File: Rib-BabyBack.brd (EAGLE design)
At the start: 67.3 x 74.9 mm, 30 parts, among them IC1 REG1117, SW1 DPDT

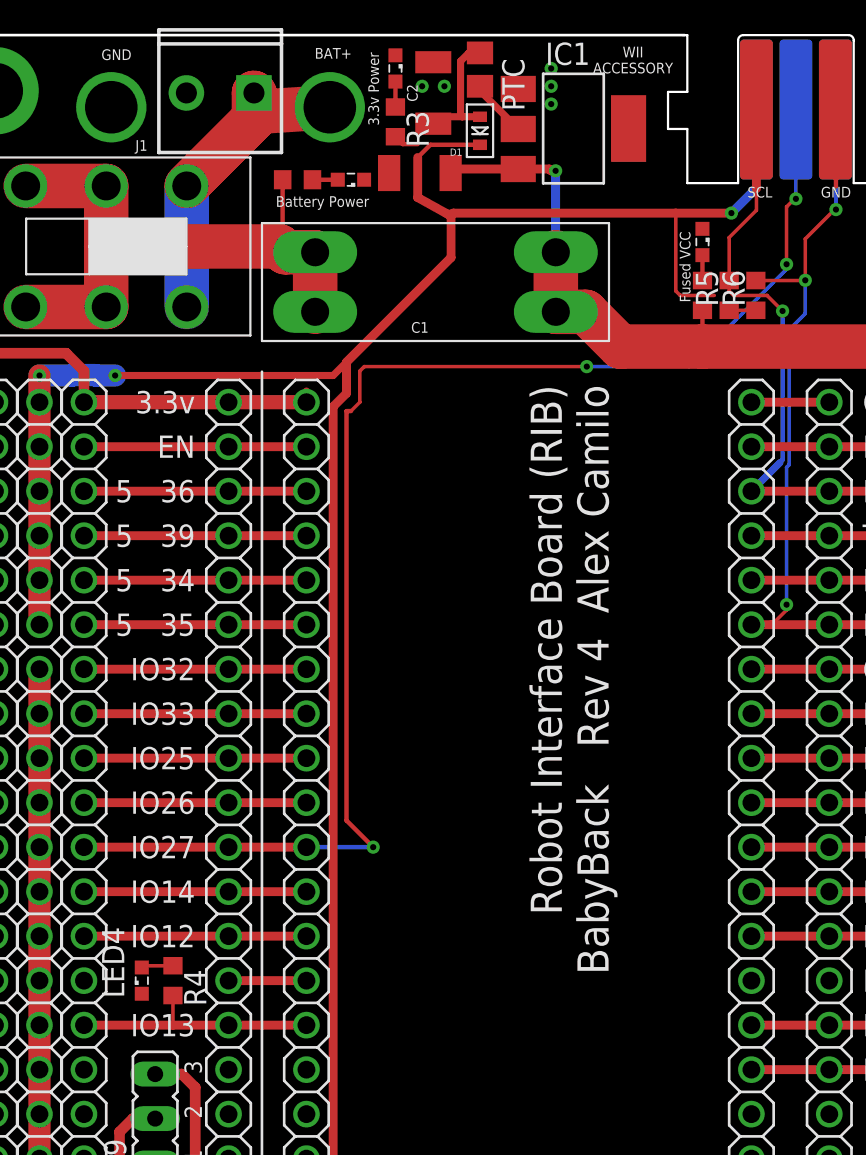
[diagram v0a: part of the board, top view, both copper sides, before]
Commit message: Resolved issue 38
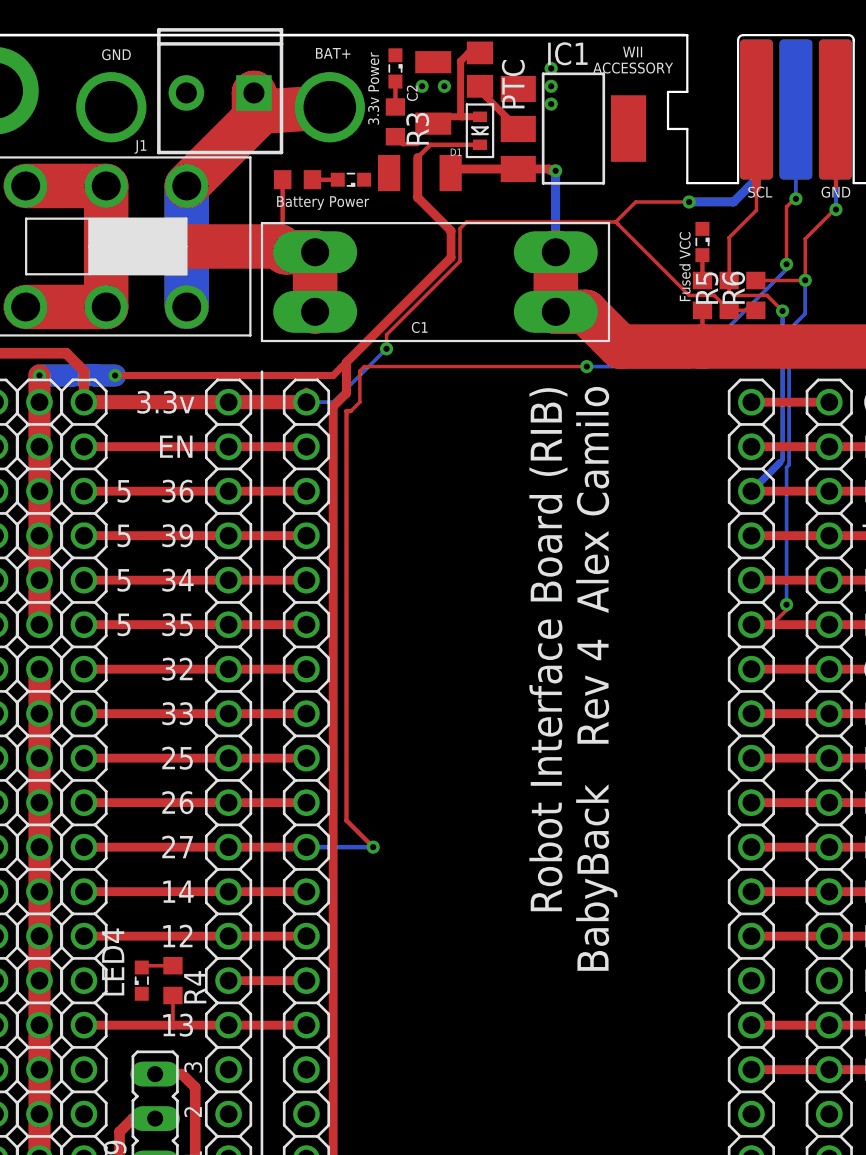
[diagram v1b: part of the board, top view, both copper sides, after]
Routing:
- net 3V3: track 90.1 -> 135.2 mm, vias 0 -> 2
- net 5V: track 141.0 -> 115.8 mm, vias 3 -> 2
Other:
- board text added: "12"
- board text added: "13"
- board text added: "14"
- board text added: "25"
- board text added: "26"
- board text added: "27"
- board text added: "32"
- board text added: "33"
- board text removed: "IO12"
- board text removed: "IO13"
- board text removed: "IO14"
- board text removed: "IO25"
- board text removed: "IO26"
- board text removed: "IO27"
- board text removed: "IO32"
- board text removed: "IO33"
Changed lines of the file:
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@@
 <text x="14.986" y="43.815" size="1.27" layer="21" font="vector" ratio="20" align="bottom-right">34</text>
 <text x="14.986" y="41.275" size="1.27" layer="21" font="vector" ratio="20" align="bottom-right">35</text>
-<text x="14.986" y="38.735" size="1.27" layer="21" font="vector" ratio="20" align="bottom-right">IO32</text>
-<text x="14.986" y="36.195" size="1.27" layer="21" font="vector" ratio="20" align="bottom-right">IO33</text>
-<text x="14.986" y="33.655" size="1.27" layer="21" font="vector" ratio="20" align="bottom-right">IO25</text>
-<text x="14.986" y="31.115" size="1.27" layer="21" font="vector" ratio="20" align="bottom-right">IO26</text>
-<text x="14.986" y="28.575" size="1.27" layer="21" font="vector" ratio="20" align="bottom-right">IO27</text>
-<text x="14.986" y="26.035" size="1.27" layer="21" font="vector" ratio="20" align="bottom-right">IO14</text>
-<text x="14.986" y="23.495" size="1.27" layer="21" font="vector" ratio="20" align="bottom-right">IO12</text>
-<text x="14.986" y="18.415" size="1.27" layer="21" font="vector" ratio="20" align="bottom-right">IO13</text>
+<text x="14.986" y="38.735" size="1.27" layer="21" font="vector" ratio="20" align="bottom-right">32</text>
+<text x="14.986" y="36.195" size="1.27" layer="21" font="vector" ratio="20" align="bottom-right">33</text>
+<text x="14.986" y="33.655" size="1.27" layer="21" font="vector" ratio="20" align="bottom-right">25</text>
+<text x="14.986" y="31.115" size="1.27" layer="21" font="vector" ratio="20" align="bottom-right">26</text>
+<text x="14.986" y="28.575" size="1.27" layer="21" font="vector" ratio="20" align="bottom-right">27</text>
+<text x="14.986" y="26.035" size="1.27" layer="21" font="vector" ratio="20" align="bottom-right">14</text>
+<text x="14.986" y="23.495" size="1.27" layer="21" font="vector" ratio="20" align="bottom-right">12</text>
+<text x="14.986" y="18.415" size="1.27" layer="21" font="vector" ratio="20" align="bottom-right">13</text>
 <text x="14.986" y="8.255" size="1.27" layer="21" font="vector" ratio="20" align="bottom-right">5v</text>
 <text x="53.086" y="53.975" size="1.27" layer="21" font="vector" ratio="20">GND</text>
@@
 <contactref element="JP6" pad="1"/>
 <wire x1="16.891" y1="8.89" x2="21.336" y2="8.89" width="0.508" layer="1"/>
-<wire x1="47.021" y1="66.833" x2="45.593" y2="65.405" width="0.508" layer="16"/>
-<via x="45.593" y="65.405" extent="1-16" drill="0.35"/>
-<wire x1="29.718" y1="65.405" x2="29.6545" y2="65.3415" width="0.508" layer="1"/>
-<wire x1="29.6545" y1="65.3415" x2="29.591" y2="65.278" width="0.508" layer="1"/>
-<wire x1="45.593" y1="65.405" x2="42.418" y2="65.405" width="0.508" layer="1"/>
-<wire x1="42.418" y1="65.405" x2="29.718" y2="65.405" width="0.508" layer="1"/>
-<wire x1="29.6545" y1="65.3415" x2="29.4005" y2="65.3415" width="0.508" layer="1"/>
-<wire x1="29.4005" y1="65.3415" x2="27.686" y2="66.294" width="0.508" layer="1"/>
 <wire x1="27.686" y1="66.294" x2="27.686" y2="68.58" width="0.508" layer="1"/>
 <contactref element="R3" pad="2"/>
@@
 <wire x1="23.622" y1="55.118" x2="23.622" y2="56.896" width="0.508" layer="1"/>
 <wire x1="23.622" y1="56.896" x2="29.591" y2="62.865" width="0.508" layer="1"/>
-<wire x1="29.591" y1="62.865" x2="29.591" y2="65.278" width="0.508" layer="1"/>
-<wire x1="44.616" y1="60.706" x2="42.672" y2="60.706" width="0.2032" layer="1"/>
-<wire x1="42.672" y1="60.706" x2="42.418" y2="60.96" width="0.2032" layer="1"/>
-<wire x1="42.418" y1="60.96" x2="42.418" y2="65.405" width="0.2032" layer="1"/>
 <wire x1="16.891" y1="8.89" x2="14.986" y2="10.795" width="0.6096" layer="1"/>
 <wire x1="14.986" y1="15.494" x2="14.986" y2="10.795" width="0.6096" layer="1"/>
@@
 <wire x1="10.414" y1="56.134" x2="22.86" y2="56.134" width="0.4064" layer="1"/>
 <wire x1="22.86" y1="56.134" x2="23.622" y2="56.896" width="0.4064" layer="1"/>
+<wire x1="29.591" y1="62.865" x2="29.591" y2="64.389" width="0.508" layer="1"/>
+<wire x1="29.591" y1="64.389" x2="27.686" y2="66.294" width="0.508" layer="1"/>
 <wire x1="28.41" y1="69.304" x2="27.686" y2="69.342" width="0" layer="19" extent="1-1"/>
 <wire x1="8.636" y1="8.89" x2="14.986" y2="10.795" width="0" layer="19" extent="1-1"/>
@@
 <wire x1="11.176" y1="5.334" x2="12.7" y2="6.858" width="0.6096" layer="1"/>
 <wire x1="12.7" y1="6.858" x2="12.7" y2="11.176" width="0.6096" layer="1"/>
-<wire x1="46.99" y1="59.856" x2="47.021" y2="71.315" width="0" layer="19" extent="1-16"/>
-<wire x1="21.336" y1="55.245" x2="45.466" y2="59.856" width="0" layer="19" extent="1-1"/>
+<wire x1="45.466" y1="59.856" x2="44.616" y2="60.706" width="0.2032" layer="1"/>
+<wire x1="44.616" y1="60.706" x2="43.18" y2="60.706" width="0.2032" layer="1"/>
+<wire x1="43.18" y1="60.706" x2="39.116" y2="64.77" width="0.2032" layer="1"/>
+<wire x1="39.116" y1="64.77" x2="38.989" y2="64.897" width="0.2032" layer="1"/>
+<wire x1="38.989" y1="64.897" x2="30.48" y2="64.897" width="0.2032" layer="1"/>
+<wire x1="30.48" y1="64.897" x2="30.099" y2="64.516" width="0.2032" layer="1"/>
+<wire x1="30.099" y1="64.516" x2="30.099" y2="62.654575" width="0.2032" layer="1"/>
+<wire x1="25.908" y1="58.463575" x2="25.908" y2="57.658" width="0.2032" layer="1"/>
+<wire x1="30.099" y1="62.654575" x2="25.908" y2="58.463575" width="0.2032" layer="1"/>
+<via x="25.908" y="57.658" extent="1-16" drill="0.35"/>
+<wire x1="25.908" y1="57.658" x2="22.86" y2="54.61" width="0.2032" layer="16"/>
+<wire x1="22.86" y1="54.61" x2="21.336" y2="54.61" width="0.2032" layer="16"/>
+<wire x1="47.021" y1="71.315" x2="47.021" y2="67.341" width="0.508" layer="16"/>
+<wire x1="47.021" y1="67.341" x2="45.72" y2="66.04" width="0.508" layer="16"/>
+<wire x1="45.72" y1="66.04" x2="43.18" y2="66.04" width="0.508" layer="16"/>
+<via x="43.18" y="66.04" extent="1-16" drill="0.35"/>
+<wire x1="43.18" y1="66.04" x2="40.132" y2="66.04" width="0.2032" layer="1"/>
+<wire x1="40.132" y1="66.04" x2="38.989" y2="64.897" width="0.2032" layer="1"/>
 </signal>
 <signal name="SENSORV">

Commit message: Resolved issue 31
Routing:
- net TX0: track 35.1 -> 12.7 mm, vias 1 -> 0
- net RX0: track 34.7 -> 12.7 mm, vias 1 -> 0
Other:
- board text added: "0"
- board text added: "15"
- board text added: "16"
- board text added: "17"
- board text added: "18"
- board text added: "19"
- board text added: "2"
- board text added: "23"
- board text added: "4"
- board text added: "S"
- board text removed: "IO0"
- board text removed: "IO15"
- board text removed: "IO16"
- board text removed: "IO17"
- board text removed: "IO18"
- board text removed: "IO19"
- board text removed: "IO2"
- board text removed: "IO21"
- board text removed: "IO22"
- board text removed: "IO23"
- board text removed: "IO4"
- board text removed: "IO5"
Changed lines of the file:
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@@
 <text x="14.986" y="8.255" size="1.27" layer="21" font="vector" ratio="20" align="bottom-right">5v</text>
 <text x="53.086" y="53.975" size="1.27" layer="21" font="vector" ratio="20">GND</text>
-<text x="53.086" y="51.435" size="1.27" layer="21" font="vector" ratio="20">IO23</text>
-<text x="53.086" y="48.895" size="1.27" layer="21" font="vector" ratio="20">IO22</text>
+<text x="53.086" y="51.435" size="1.27" layer="21" font="vector" ratio="20">23</text>
+<text x="53.086" y="48.895" size="1.27" layer="21" font="vector" ratio="20">SCL</text>
 <text x="53.086" y="46.355" size="1.27" layer="21" font="vector" ratio="20">TX0</text>
 <text x="53.086" y="43.815" size="1.27" layer="21" font="vector" ratio="20">RX0</text>
-<text x="53.086" y="41.275" size="1.27" layer="21" font="vector" ratio="20">IO21</text>
+<text x="53.086" y="41.275" size="1.27" layer="21" font="vector" ratio="20">SDA</text>
 <text x="53.086" y="38.735" size="1.27" layer="21" font="vector" ratio="20">GND</text>
-<text x="53.086" y="36.195" size="1.27" layer="21" font="vector" ratio="20">IO19</text>
-<text x="53.086" y="33.655" size="1.27" layer="21" font="vector" ratio="20">IO18</text>
-<text x="53.086" y="31.115" size="1.27" layer="21" font="vector" ratio="20">IO5</text>
-<text x="53.086" y="28.575" size="1.27" layer="21" font="vector" ratio="20">IO17</text>
-<text x="53.086" y="26.035" size="1.27" layer="21" font="vector" ratio="20">IO16</text>
-<text x="53.086" y="23.495" size="1.27" layer="21" font="vector" ratio="20">IO4</text>
-<text x="53.086" y="20.955" size="1.27" layer="21" font="vector" ratio="20">IO0</text>
-<text x="53.086" y="18.415" size="1.27" layer="21" font="vector" ratio="20">IO2</text>
-<text x="53.086" y="15.875" size="1.27" layer="21" font="vector" ratio="20">IO15</text>
+<text x="53.086" y="36.195" size="1.27" layer="21" font="vector" ratio="20">19</text>
+<text x="53.086" y="33.655" size="1.27" layer="21" font="vector" ratio="20">18</text>
+<text x="53.086" y="31.115" size="1.27" layer="21" font="vector" ratio="20">5</text>
+<text x="53.086" y="28.575" size="1.27" layer="21" font="vector" ratio="20">17</text>
+<text x="53.086" y="26.035" size="1.27" layer="21" font="vector" ratio="20">16</text>
+<text x="53.086" y="23.495" size="1.27" layer="21" font="vector" ratio="20">4</text>
+<text x="53.086" y="20.955" size="1.27" layer="21" font="vector" ratio="20">0</text>
+<text x="53.086" y="18.415" size="1.27" layer="21" font="vector" ratio="20">2</text>
+<text x="53.086" y="15.875" size="1.27" layer="21" font="vector" ratio="20">15</text>
 <wire x1="49.276" y1="7.15" x2="18.836" y2="7.15" width="0.1524" layer="22"/>
 <wire x1="49.276" y1="7.15" x2="49.276" y2="56.35" width="0.1524" layer="22"/>
@@
 <text x="11.43" y="43.815" size="1.27" layer="21" font="vector" ratio="20" align="bottom-right">5</text>
 <text x="11.43" y="41.275" size="1.27" layer="21" font="vector" ratio="20" align="bottom-right">5</text>
+<text x="56.642" y="15.875" size="1.27" layer="21" font="vector" ratio="20">S</text>
+<text x="56.642" y="18.415" size="1.27" layer="21" font="vector" ratio="20">S</text>
+<text x="56.642" y="20.955" size="1.27" layer="21" font="vector" ratio="20">S</text>
+<text x="56.642" y="23.495" size="1.27" layer="21" font="vector" ratio="20">S</text>
+<text x="56.642" y="26.035" size="1.27" layer="21" font="vector" ratio="20">S</text>
+<text x="56.642" y="28.575" size="1.27" layer="21" font="vector" ratio="20">S</text>
+<text x="56.642" y="31.115" size="1.27" layer="21" font="vector" ratio="20">S</text>
+<text x="56.642" y="33.655" size="1.27" layer="21" font="vector" ratio="20">S</text>
+<text x="56.642" y="36.195" size="1.27" layer="21" font="vector" ratio="20">S</text>
+<text x="56.642" y="51.435" size="1.27" layer="21" font="vector" ratio="20">S</text>
 </plain>
 <attributes>
@@
 <wire x1="46.736" y1="44.45" x2="51.181" y2="44.45" width="0.508" layer="1"/>
 <wire x1="51.181" y1="44.45" x2="59.436" y2="44.45" width="0.508" layer="1"/>
-<wire x1="59.436" y1="44.45" x2="60.0202" y2="44.45" width="0.1524" layer="16"/>
-<wire x1="60.0202" y1="44.45" x2="61.214" y2="45.6438" width="0.1524" layer="16"/>
-<wire x1="61.214" y1="45.6438" x2="65.9892" y2="45.6438" width="0.1524" layer="16"/>
-<wire x1="65.9892" y1="45.6438" x2="66.1924" y2="45.847" width="0.1524" layer="16"/>
-<wire x1="66.1924" y1="45.847" x2="66.2178" y2="45.847" width="0.1524" layer="16"/>
-<via x="66.2178" y="45.847" extent="1-16" drill="0.35"/>
-<wire x1="66.2178" y1="45.847" x2="66.2178" y2="33.1216" width="0.1524" layer="1"/>
-<wire x1="67.5894" y1="31.75" x2="66.2178" y2="33.1216" width="0.1524" layer="1"/>
 </signal>
 <signal name="TX0">
@@
 <wire x1="59.436" y1="46.99" x2="51.181" y2="46.99" width="0.508" layer="1"/>
 <wire x1="51.181" y1="46.99" x2="46.736" y2="46.99" width="0.508" layer="1"/>
-<wire x1="59.436" y1="46.99" x2="60.1218" y2="46.99" width="0.1524" layer="16"/>
-<wire x1="60.1218" y1="46.99" x2="61.1632" y2="45.9486" width="0.1524" layer="16"/>
-<wire x1="61.1632" y1="45.9486" x2="65.405" y2="45.9486" width="0.1524" layer="16"/>
-<wire x1="65.405" y1="45.9486" x2="66.1924" y2="46.736" width="0.1524" layer="16"/>
-<wire x1="66.1924" y1="46.736" x2="66.2178" y2="46.8884" width="0.1524" layer="16"/>
-<via x="66.2178" y="46.8884" extent="1-16" drill="0.35"/>
-<wire x1="66.8246" y1="46.09835" x2="66.8246" y2="45.59565" width="0.1524" layer="1"/>
-<wire x1="66.8246" y1="45.59565" x2="66.5226" y2="45.29365" width="0.1524" layer="1"/>
-<wire x1="66.2178" y1="46.8884" x2="66.2178" y2="46.70515" width="0.1524" layer="1"/>
-<wire x1="66.2178" y1="46.70515" x2="66.8246" y2="46.09835" width="0.1524" layer="1"/>
-<wire x1="67.7192" y1="32.9918" x2="66.5226" y2="34.1884" width="0.1524" layer="1"/>
-<wire x1="66.5226" y1="45.29365" x2="66.5226" y2="34.1884" width="0.1524" layer="1"/>
 </signal>
 <signal name="VCC">
